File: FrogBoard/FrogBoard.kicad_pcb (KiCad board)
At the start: 2 copper layers, 59.3 x 50.6 mm, 38 parts, among them J1 Conn_01x10, J2 Conn_01x04, J3 USB_B_Micro, J4 Stickbox, J5 Conn_01x03_Socket, J6 Conn_01x02, J7 Conn_01x02, U1 STM32L432KBUx, U2 USBLC6-2P6, U3 MCP1700T-3302E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

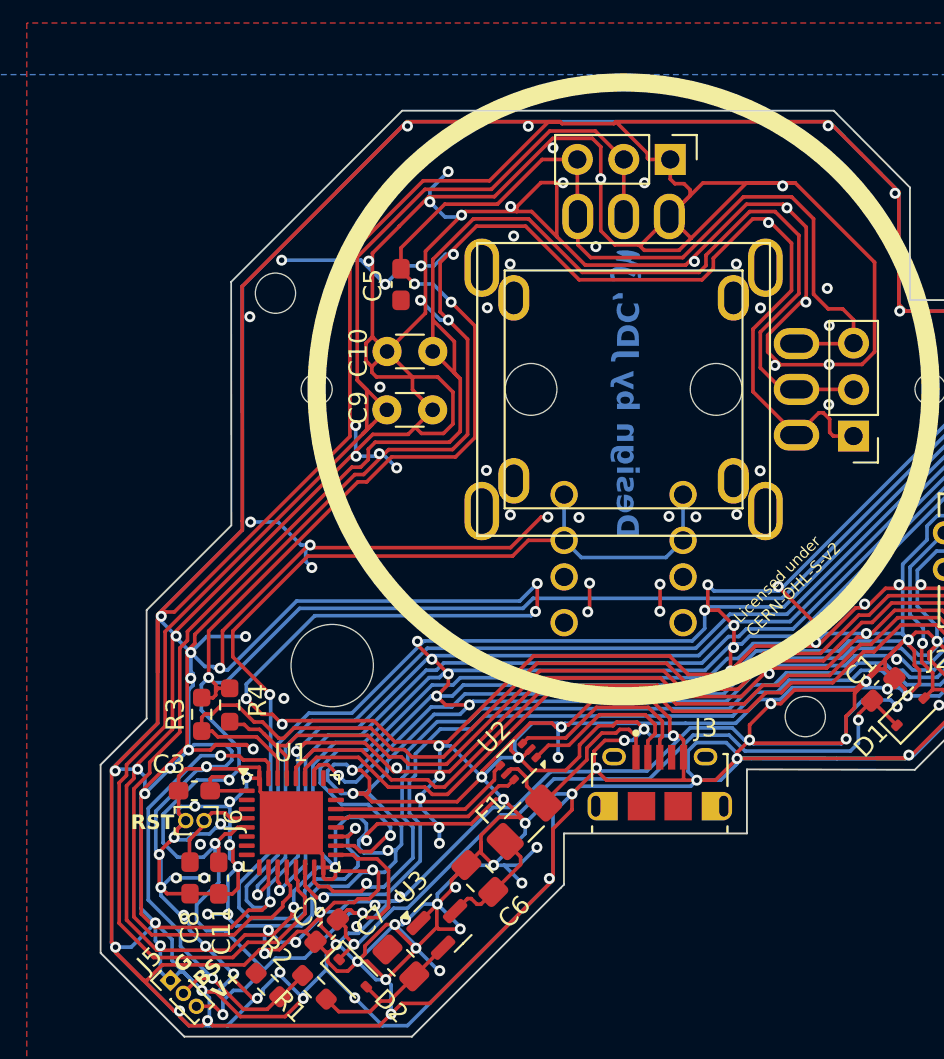
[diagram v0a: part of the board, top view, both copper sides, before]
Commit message: Add notch in board outline for johnny's case; 3d model test
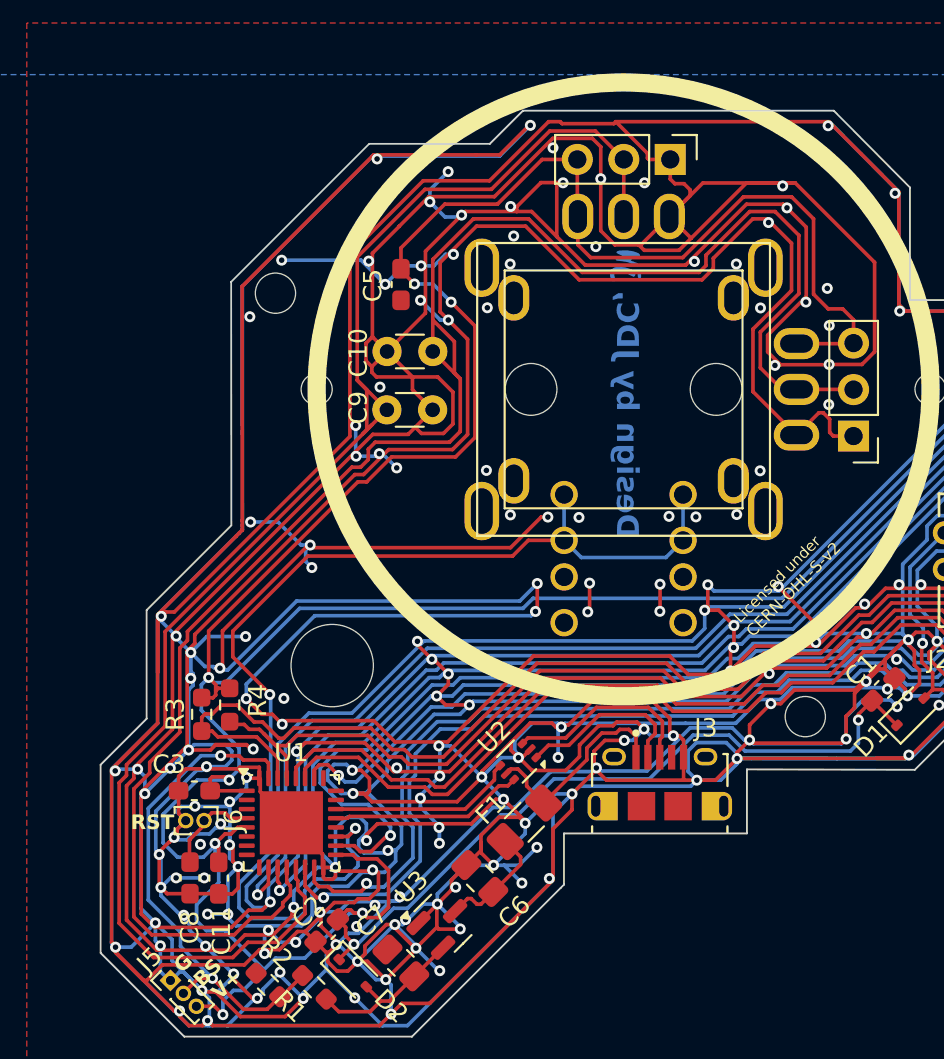
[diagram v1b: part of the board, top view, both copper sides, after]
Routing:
- net GND: track 1778.2 -> 1760.1 mm
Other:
- outline, holes or cut-outs redrawn

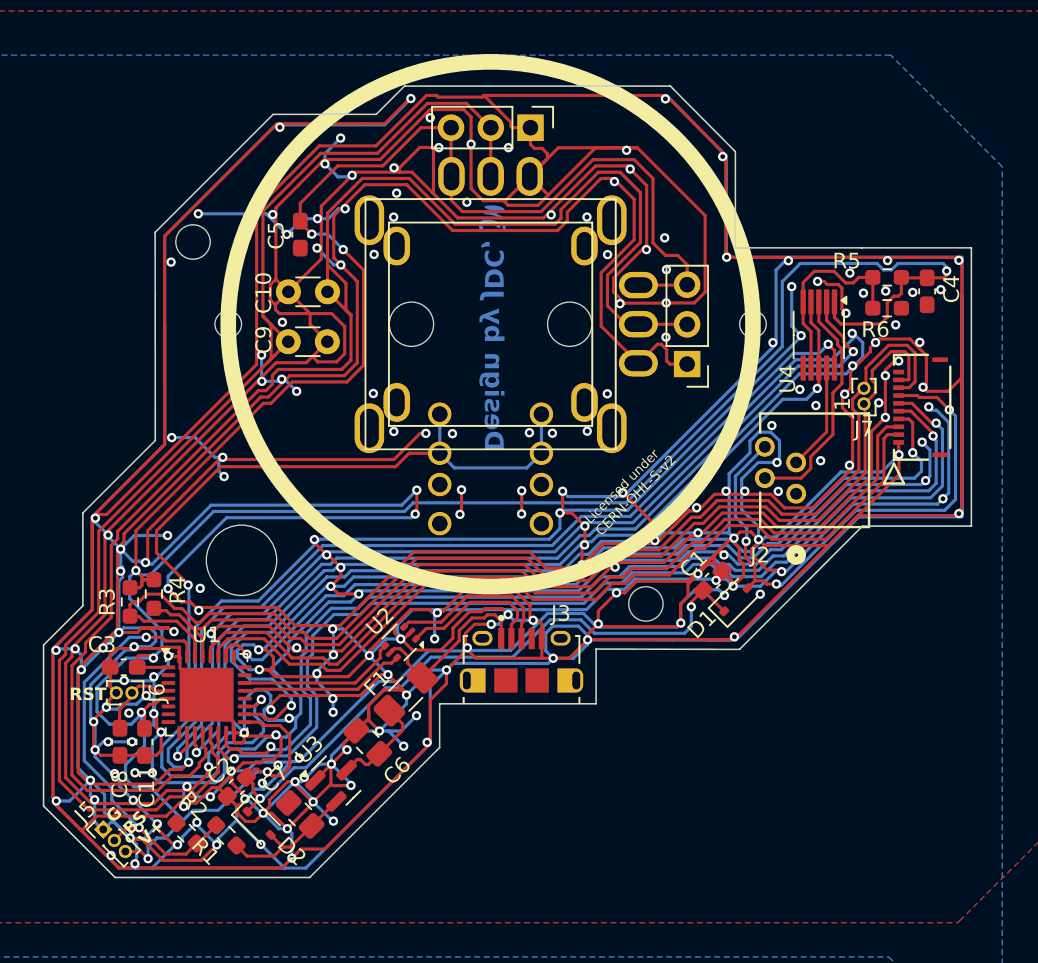
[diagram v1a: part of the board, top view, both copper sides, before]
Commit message: more ground cleanups and stitching
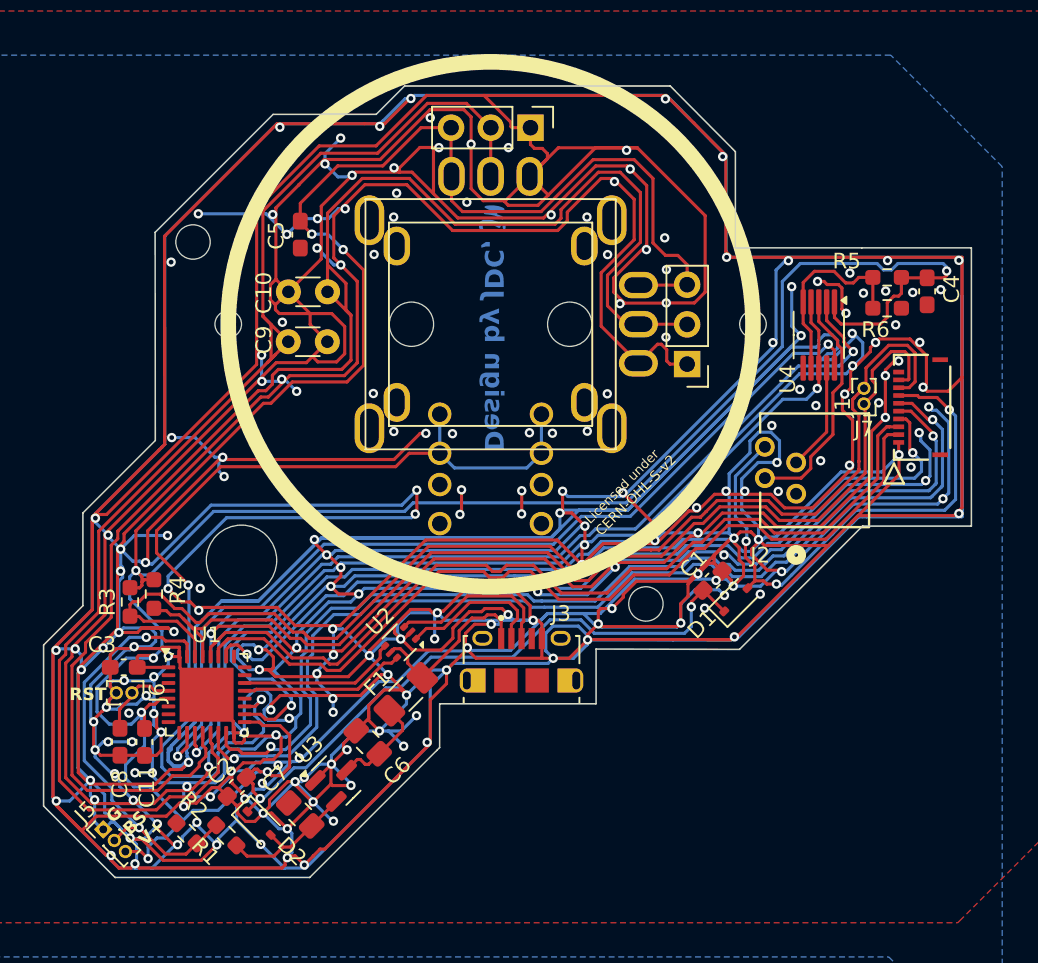
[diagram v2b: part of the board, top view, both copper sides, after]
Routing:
- net GND: track 1760.1 -> 1813.8 mm, vias 220 -> 227
- net FFC_P3: track 55.3 -> 56.2 mm
- net FFC_P2: track 54.5 -> 55.5 mm
- net SDA: track 75.1 -> 75.8 mm
- net SCL: track 67.9 -> 68.5 mm

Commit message: more refinement, also added DRC exclussions
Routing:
- net GND: track 1813.8 -> 1907.3 mm, vias 227 -> 248
- net SCL: track 68.5 -> 71.6 mm
- net SDA: track 75.8 -> 78.8 mm
- net FFC_P2: track 55.5 -> 58.0 mm
- net FFC_P3: track 56.2 -> 58.7 mm
- net /USB_RAW-: track 9.63 -> 7.69 mm
- net /USB_RAW+: track 10.8 -> 9.12 mm
- net +3.3V: track 247.8 -> 249.2 mm
- net AX_OUT: track 59.8 -> 61.0 mm
- net AY_OUT: track 61.2 -> 62.4 mm
- net A_SEL: track 59.7 -> 60.9 mm
- net FFC_P4: track 55.6 -> 56.4 mm
- net VBUS: track 11.6 -> 11.0 mm

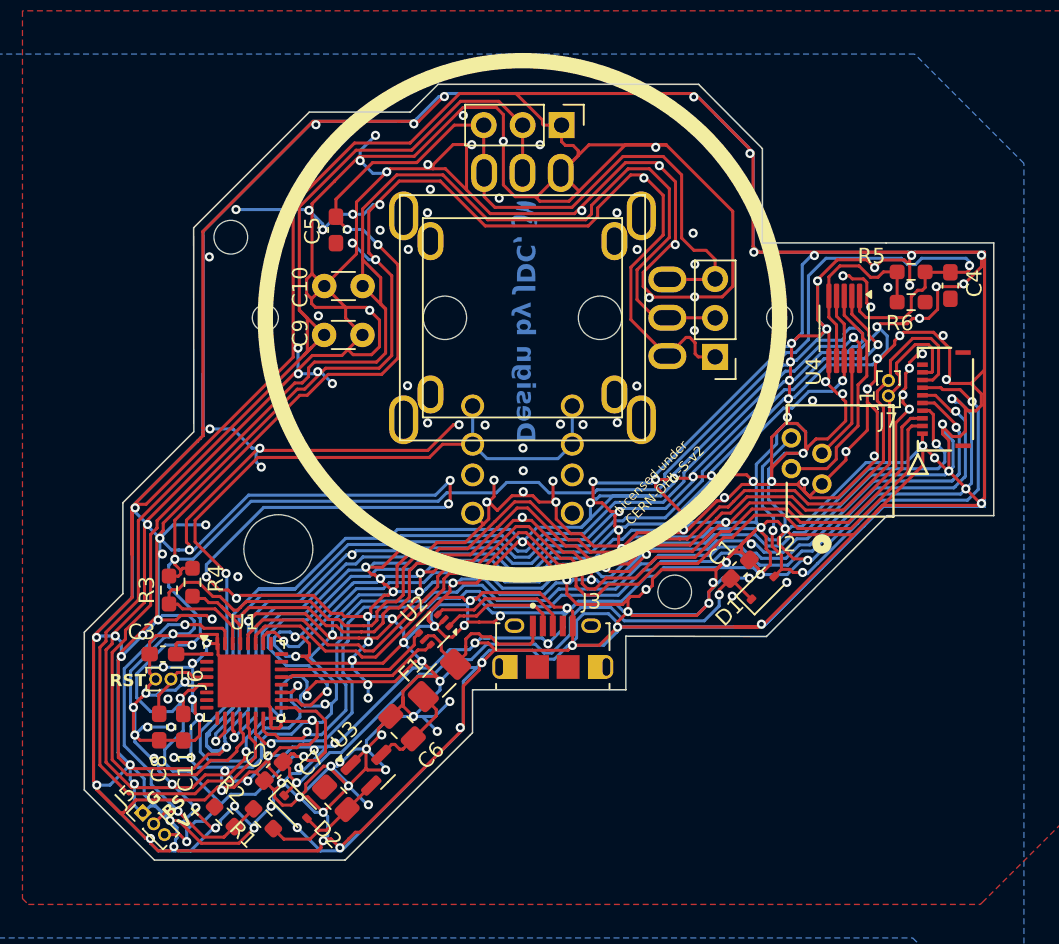
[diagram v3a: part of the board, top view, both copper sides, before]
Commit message: removed filter-cap positions and added testpoints for unused MCU pins
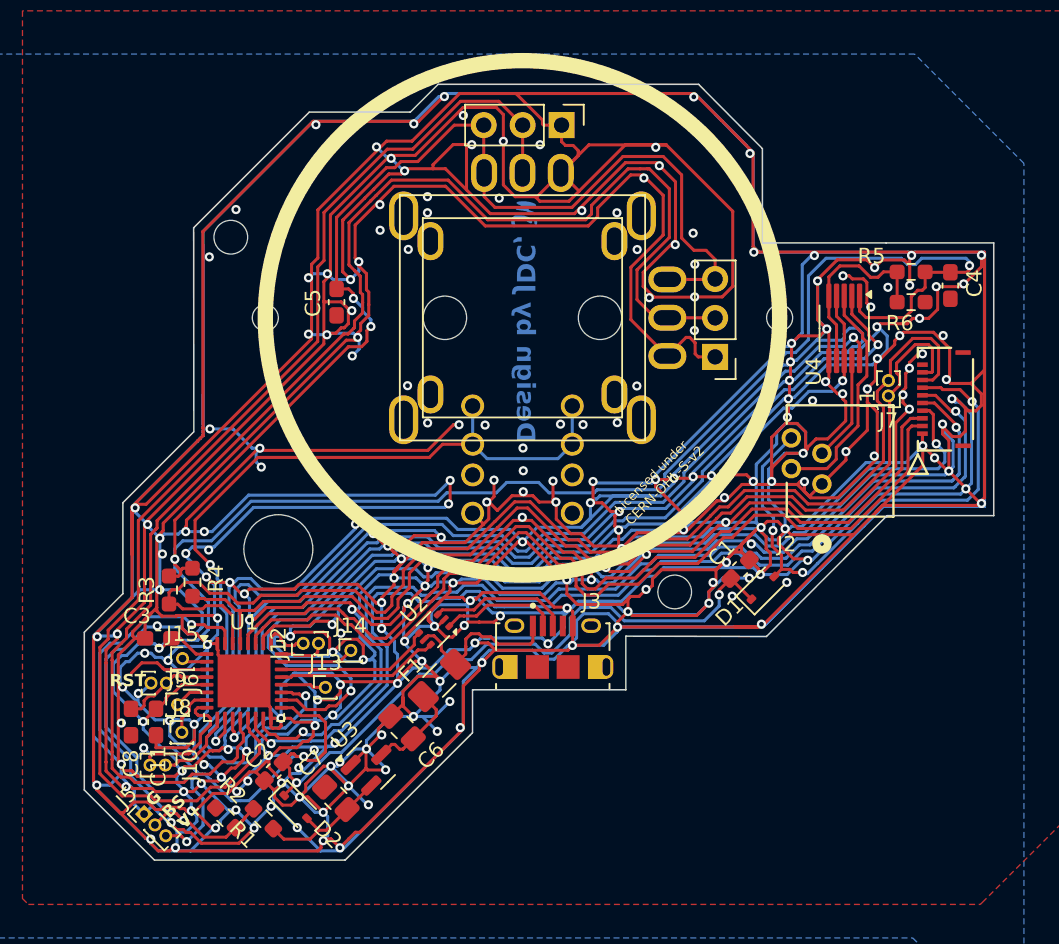
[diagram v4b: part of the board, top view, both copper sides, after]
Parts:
- removed C10, C9: ~, Capacitor_THT:C_Disc_D3.0mm_W1.6mm_P2.50mm
- added J10: Conn_01x02, FrogBoard_footprints:PinHeader_1x02_P1.00mm_Vertical_Neutral_No_Coutryard, F.Cu at (128.5, 118.4)
- added J12: Conn_01x02, FrogBoard_footprints:PinHeader_1x02_P1.00mm_Vertical_Neutral_No_Coutryard, F.Cu at (137.5, 110.5)
- added J13: Conn_01x01, FrogBoard_footprints:FrogBoard_PinHeader_1x01_P1.00mm_Vertical, F.Cu at (138.9, 113.3)
- added J14: Conn_01x01, FrogBoard_footprints:FrogBoard_PinHeader_1x01_P1.00mm_Vertical, F.Cu at (140.6, 110.9)
- added J15: Conn_01x01, FrogBoard_footprints:FrogBoard_PinHeader_1x01_P1.00mm_Vertical, F.Cu at (129.6, 111.5)
- added J8: Conn_01x01, FrogBoard_footprints:FrogBoard_PinHeader_1x01_P1.00mm_Vertical, F.Cu at (129.5, 116.3)
- added J9: Conn_01x01, FrogBoard_footprints:FrogBoard_PinHeader_1x01_P1.00mm_Vertical, F.Cu at (129.3, 114.5)
- moved C5 4.71 mm to (139.6, 88.2)
- moved C8 1.87 mm to (126.2, 115.6)
- moved C11 1.81 mm to (127.8, 115.6)
- moved C3 1.07 mm to (128.0, 110.1)
- moved J6 0.40 mm to (128.5, 113.1)
- moved J5 0.11 mm to (127.1, 121.6)
- moved R2 0.10 mm to (132.4, 121.8)
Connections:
- U1 pad 2: unconnected-(U1-PC14-Pad2) -> Unused_9
- U1 pad 20: unconnected-(U1-PA10-Pad20) -> Unused_5
- U1 pad 23: unconnected-(U1-PA13-Pad23) -> Unused_6
- U1 pad 24: unconnected-(U1-PA14-Pad24) -> Unused_7
- U1 pad 25: unconnected-(U1-PA15-Pad25) -> Unused_8
- U1 pad 3: unconnected-(U1-PC15-Pad3) -> Unused_10
- U1 pad 6: unconnected-(U1-PA0-Pad6) -> Unused_1
- U1 pad 7: unconnected-(U1-PA1-Pad7) -> Unused_2
- U1 pad 8: unconnected-(U1-PA2-Pad8) -> Unused_3
- U1 pad 9: unconnected-(U1-PA3-Pad9) -> Unused_4
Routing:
- net GND: track 1907.3 -> 1898.2 mm, vias 248 -> 242
- net Unused_3: track 0.00 -> 8.21 mm
- net AY_IN: track 100.1 -> 94.0 mm
- net Unused_10: track 0.00 -> 5.40 mm
- net Unused_4: track 0.00 -> 5.27 mm
- net AX_IN: track 82.4 -> 77.4 mm
- net Unused_6: track 0.00 -> 4.83 mm
- net BOOT_SEL: track 27.9 -> 32.3 mm
- net A_SEL: track 60.9 -> 65.2 mm
- net Unused_2: track 0.00 -> 3.32 mm
- net Unused_7: track 0.00 -> 3.17 mm
- net Unused_8: track 0.00 -> 3.09 mm
- net Unused_5: track 0.00 -> 2.84 mm
- net AX_OUT: track 61.0 -> 63.6 mm
- net Unused_1: track 0.00 -> 2.23 mm
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
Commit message: Add LED
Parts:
- added D3: LED, LED_SMD:LED_0603_1608Metric, F.Cu at (121.7, 113.7)
- added R7: R, Resistor_SMD:R_0603_1608Metric, F.Cu at (121.7, 116.3)
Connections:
- U1 pad 8: Unused_3 -> unconnected-(R7-Pad1)
- U1 pad 9: Unused_4 -> unconnected-(U1-PA3-Pad9)

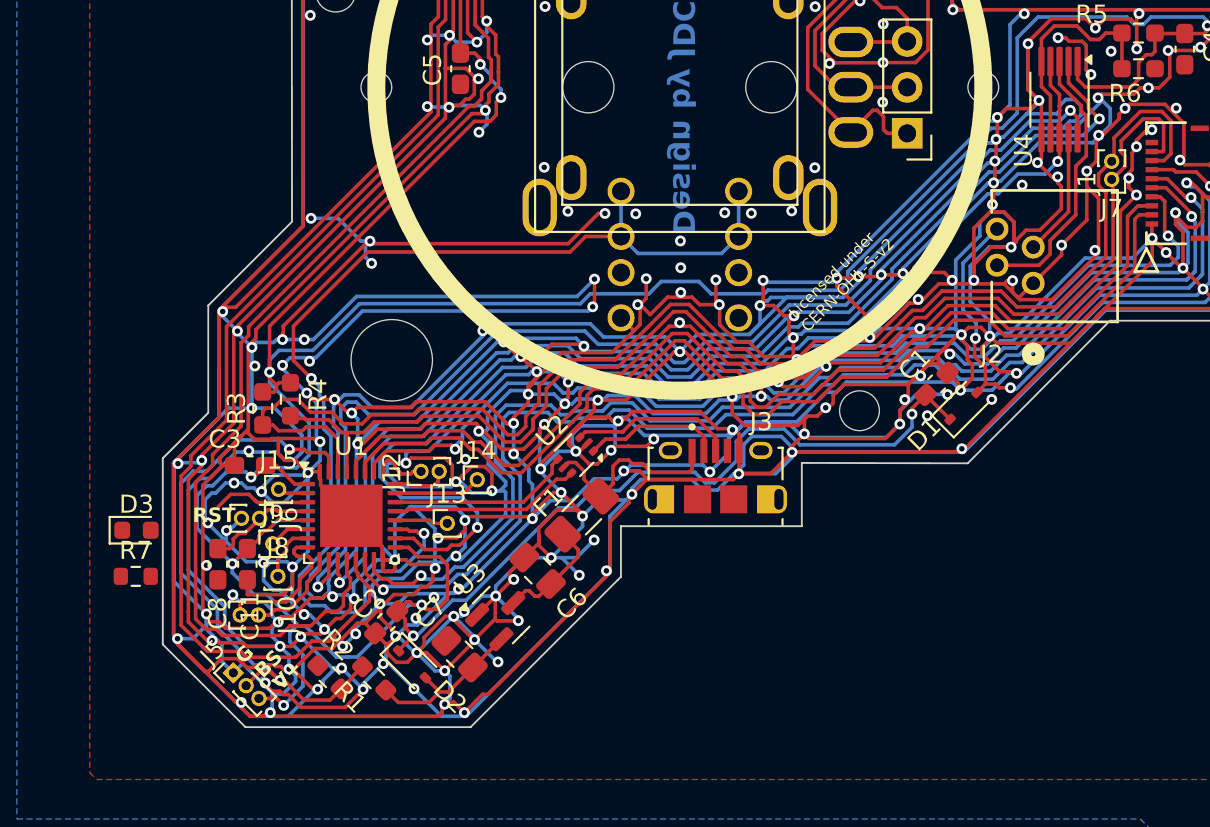
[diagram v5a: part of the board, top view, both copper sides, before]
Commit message: adding indicator LED
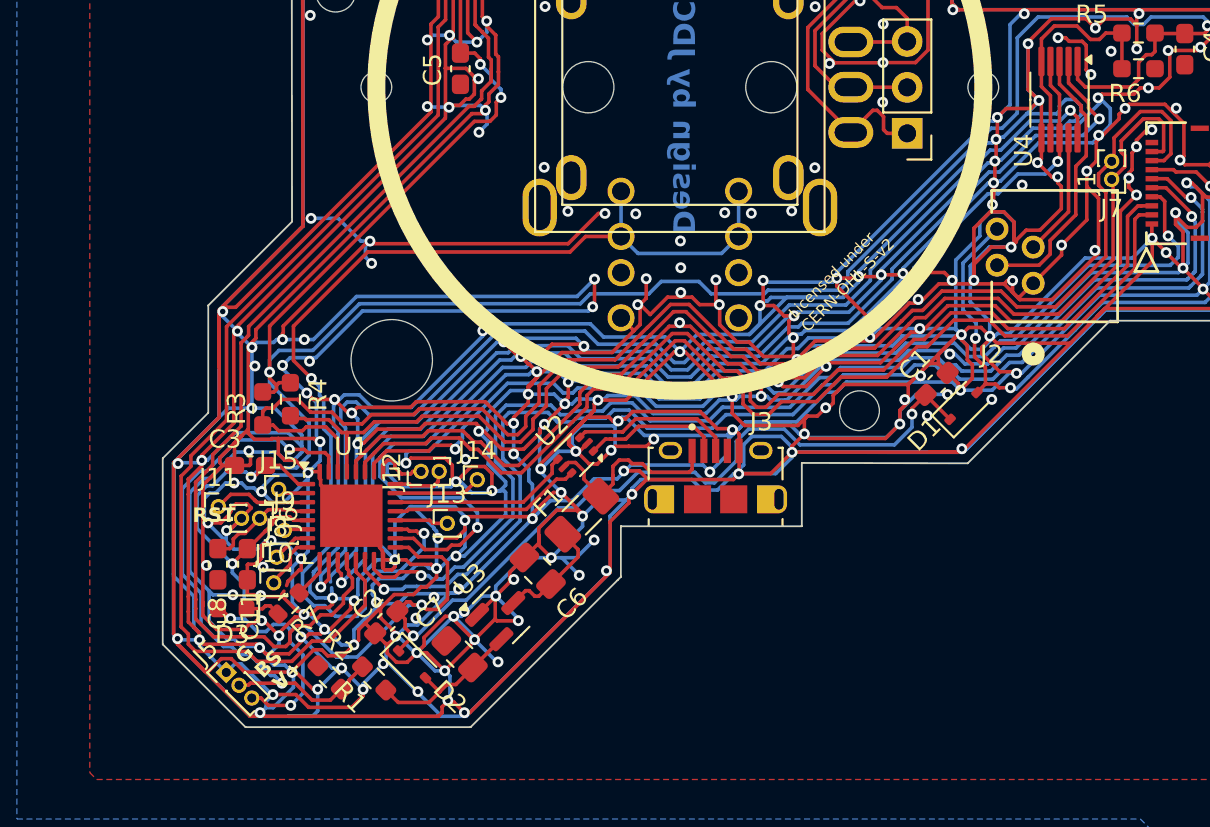
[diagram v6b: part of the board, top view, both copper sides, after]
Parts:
- added J11: Conn_01x01, FrogBoard_footprints:FrogBoard_PinHeader_1x01_P1.00mm_Vertical, F.Cu at (126.2, 112.4)
- J10: value Conn_01x02 -> Conn_01x01; footprint FrogBoard_footprints:PinHeader_1x02_P1.00mm_Vertical_Neutral_No_Coutryard -> FrogBoard_footprints:FrogBoard_PinHeader_1x01_P1.00mm_Vertical
- moved R7 8.58 mm to (130.1, 117.8), turned to -135 degrees
- moved D3 6.85 mm to (127.0, 118.1), turned to 180 degrees
- moved J10 1.97 mm to (129.3, 116.6), turned to 0 degrees
- moved J8 1.06 mm to (129.5, 115.2)
- moved J9 0.98 mm to (129.9, 113.7)
- moved J5 0.39 mm to (126.7, 121.6)
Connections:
- D3 pad 1: GND -> Net-(D3-K)
- D3 pad 2: Net-(D3-A) -> +3.3V
- J10 pad 1: Unused_4 -> Unused_3
- R7 pad 1: unconnected-(R7-Pad1) -> Net-(U1-PA3)
- R7 pad 2: Net-(D3-A) -> Net-(D3-K)
- U1 pad 8: unconnected-(R7-Pad1) -> Unused_3
- U1 pad 9: unconnected-(U1-PA3-Pad9) -> Net-(U1-PA3)
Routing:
- net GND: track 1898.2 -> 1911.2 mm
- net Unused_4: track 5.27 -> 0.00 mm
- net Unused_3: track 8.21 -> 3.03 mm
- net +3.3V: track 248.7 -> 252.0 mm, vias 10 -> 11
- net Net-(U1-PA3): track 0.00 -> 2.30 mm
- net Net-(D3-K): track 0.00 -> 1.96 mm
- net Unused_2: track 3.32 -> 2.14 mm
- net Unused_1: track 2.23 -> 1.29 mm
- net AY_IN: track 94.0 -> 94.8 mm
